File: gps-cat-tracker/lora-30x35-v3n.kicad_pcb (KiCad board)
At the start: 2 copper layers, 31 x 35 mm, 22 parts, among them J1 JST-GH_1.25mm_2P, J2 USB_C_Charge, SW1 MSK12C02, U1 E220-900T22S(JP), U2 ATtiny3226-MFR_VQFN20, U3 MAX-M8Q-00B_LCC18, U4 TP4056

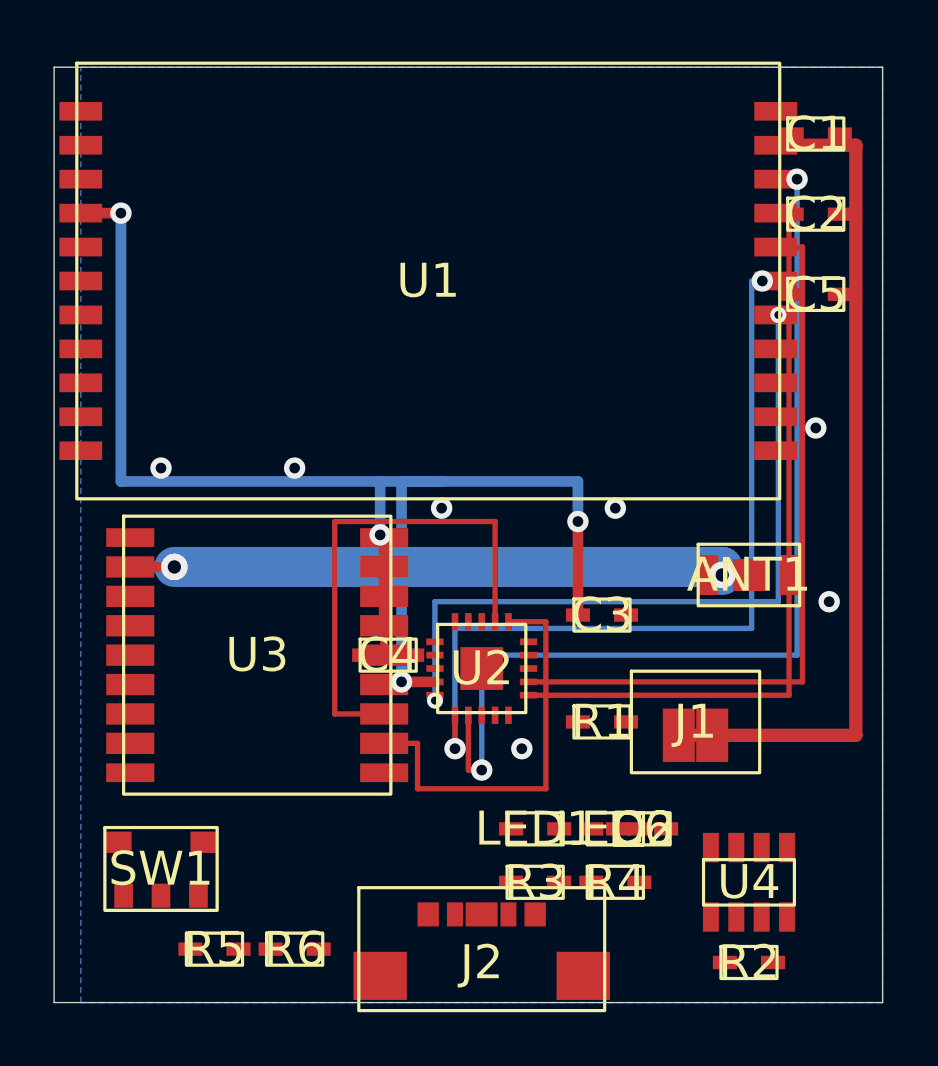
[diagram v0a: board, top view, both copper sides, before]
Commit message: v3n: GNDトレース追加・R1 DNP・B.Cuゾーン塗りつぶし・Gerber更新
- U1.pad11 GND: F.Cu トレース(26.0,1.65)→(27.5,1.65) + ビア追加
- U3 GPS左列 GND: F.Cu トレース(1.85,17.6)→(1.85,26.4) 0.5mm幅追加
- R1(10kΩ) をBOM/CPLから削除（DNP）
- B.Cu GNDゾーン塗りつぶし実行・保存
- Gerber一式再生成（gerber_v3n/）・ZIP更新

Co-Authored-By: Claude Sonnet 4.6 <noreply@anthropic.com>
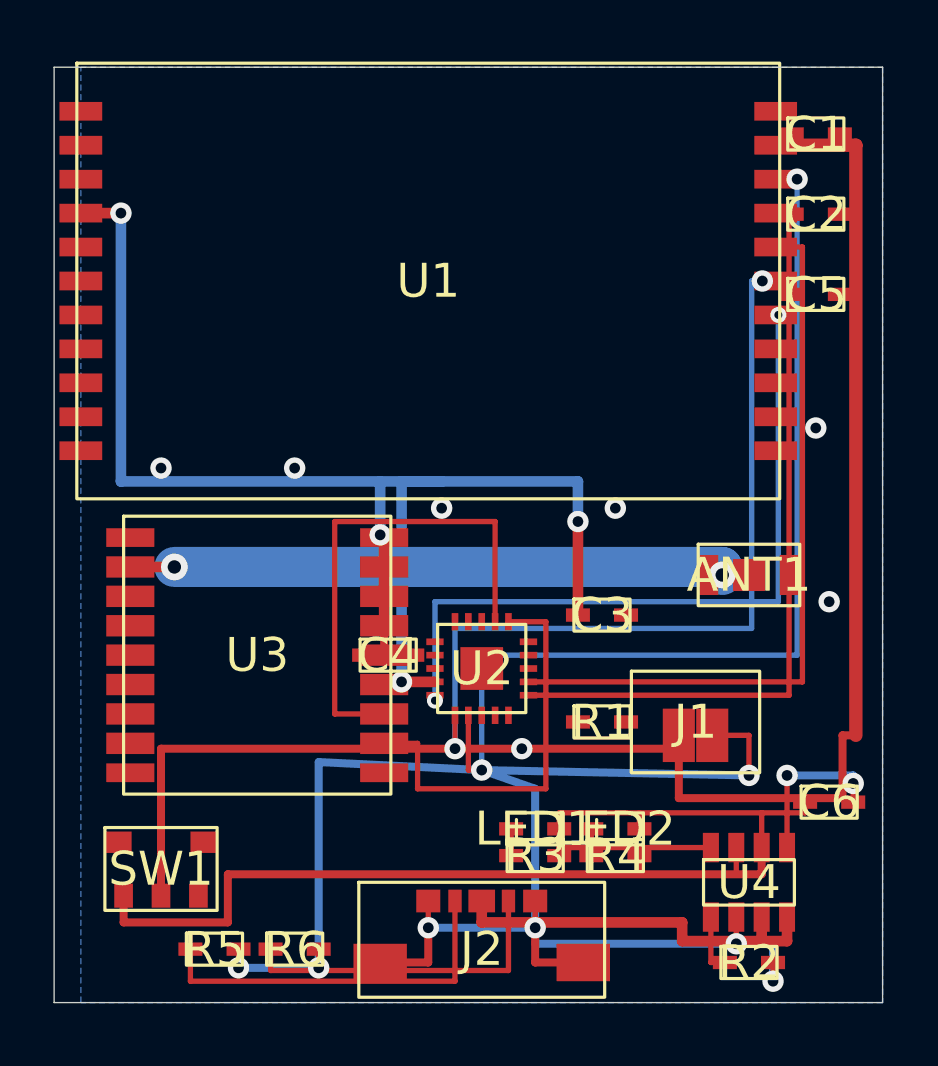
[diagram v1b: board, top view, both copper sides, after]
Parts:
- U3: value MAX-M8Q-00B_LCC18 -> ATGM336H-5N31
- moved C6 7.07 mm to (28.0, 27.5)
- moved R3 1.00 mm to (17.0, 29.5)
- moved R4 1.00 mm to (20.0, 29.5)
- moved J2 0.50 mm to (15.0, 33.0)
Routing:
- net (no net): track 290.1 -> 486.5 mm, vias 19 -> 28
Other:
- board text added: "J2.CC1(A5)→R5(5.1k)→GND / CC2(B5)→R6(5.1k)→GND"
- board text added: "J2.VBUS(AB4)→U4.VCC(3) / J2.GND(A1,B1)→GND"
- board text added: "U4.BAT(6)→SW1.pin1 / SW1.pin2→J1.BATT+→E220.VCC"
- board text added: "U4.CE(4)→VCC / TEMP(5)→GND / C6(100nF)→U4.VCC近傍"
- board text added: "U4.CHRG(8)→R3(330R)→LED1(-) LED1(+)→U4.BAT(VBAT≈3.7V)"
- board text added: "U4.PROG(1)→R2(5k)→GND [1000/5000=200mA]"
- board text added: "U4.STDBY(7)→R4(100R)→LED2(-) LED2(+)→U4.BAT(VBAT≈3.7V) ★R4=100Ω"
- board text removed: "J2.CC1(A5)→R5→GND"
- board text removed: "J2.CC2(B5)→R6→GND"
- board text removed: "J2.GND→GND"
- board text removed: "J2.VBUS→U4.VCC(3)"
- board text removed: "SW1.pin2→J1.BATT+ SW1.pin3=NC"
- board text removed: "U4.BAT(6)→SW1.pin1→J1.BATT+→E220.VCC"
- board text removed: "U4.CE(4)→VCC / TEMP(5)→GND"
- board text removed: "U4.CHRG(8)→R3→LED1(-) / LED1(+)→VCC"
- board text removed: "U4.PROG(1)→R2(5k)→GND [200mA]"
- board text removed: "U4.STDBY(7)→R4→LED2(-) / LED2(+)→VCC"

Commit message: v3n: Bug1/Bug3修正・C2/C4/C5位置修正・DRC 363→349件
- Bug1: via(13.25,23.7) + B.Cu trace(13.25,20→23.7) 削除（ATtiny pad5短絡）
- Bug3: B.Cu (12,15.5)→(12,23) を F.Cu迂回に分割（B.Cu RF/VCC交差解消）
- C4: (11.5,22,0°)→(12.9,17,90°) U3.pad5との0mm接触を解消
- C2: (27.5,5.5,0°)→(28.5,4.5,90°) U1.pad8との0mm接触を解消
- C5: (27.5,8.5,0°)→(28.5,7.5,90°) U1.pad6との0mm接触を解消
- 各バイパスコンデンサにVCC/GNDトレース追加
- 孤立via×6削除・デッドエンドトレース×3削除
- DRC: clearance 10→2件、via_dangling 4→0件

Co-Authored-By: Claude Sonnet 4.6 <noreply@anthropic.com>
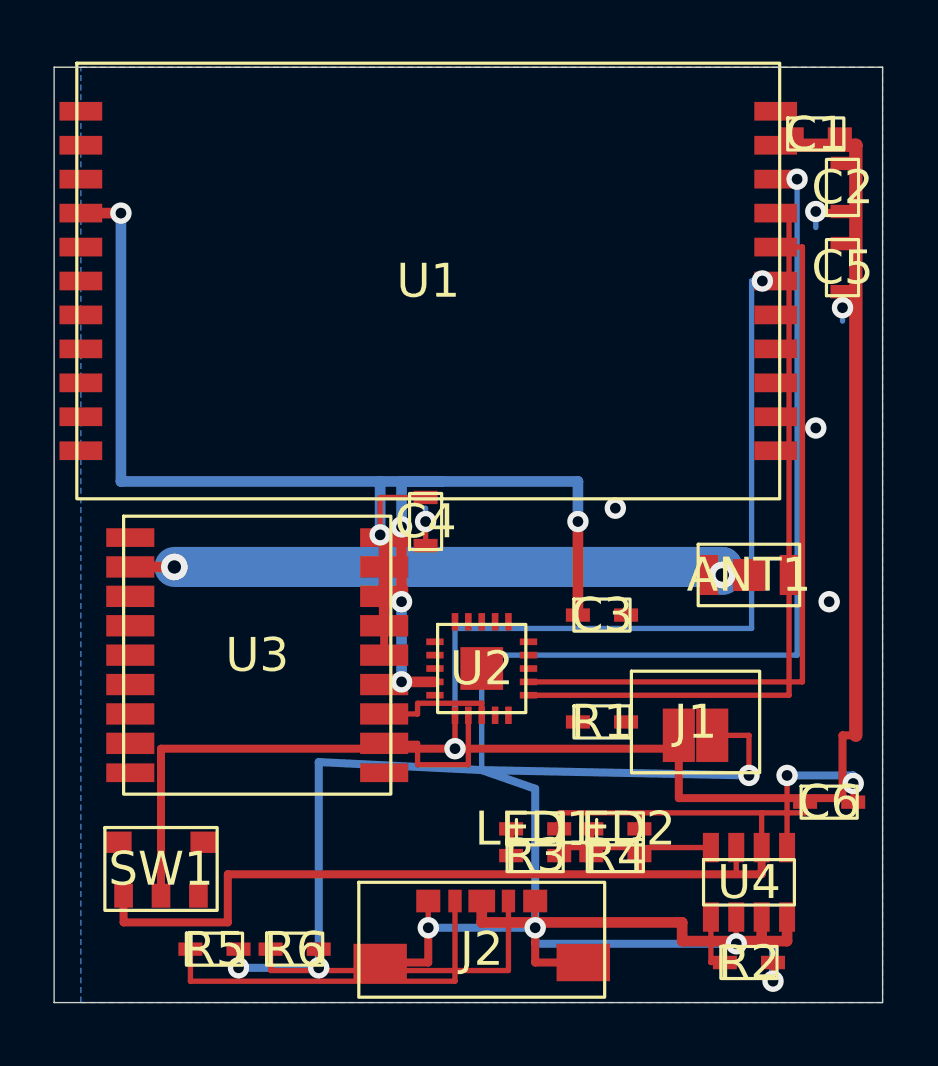
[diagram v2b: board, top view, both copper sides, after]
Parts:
- moved C4 5.19 mm to (12.9, 17.0), turned to 90 degrees
- moved C2 1.41 mm to (28.5, 4.50), turned to 90 degrees
- moved C5 1.41 mm to (28.5, 7.50), turned to 90 degrees
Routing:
- net (no net): track 486.5 -> 440.1 mm, vias 28 -> 26
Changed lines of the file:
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@@
 	(footprint ""
 		(layer "F.Cu")
-		(at 11.5 22)
+		(at 12.9 17 90)
 		(property "Reference" "C4"
 			(at 0 0 0)
@@
 	(footprint ""
 		(layer "F.Cu")
-		(at 27.5 5.5)
+		(at 28.5 4.5 90)
 		(property "Reference" "C2"
 			(at 0 0 0)
@@
 	(footprint ""
 		(layer "F.Cu")
-		(at 27.5 8.5)
+		(at 28.5 7.5 90)
 		(property "Reference" "C5"
 			(at 0 0 0)
@@
 	)
 	(segment
+		(start 15 23.8)
+		(end 15 24.25)
+		(width 0.2)
+		(layer "F.Cu")
+		(net "")
+	)
+	(segment
 		(start 27.1 27.9)
 		(end 27.1 27.5)
@@
 	)
 	(segment
+		(start 12.9 17.9)
+		(end 12.9 17)
+		(width 0.2)
+		(layer "F.Cu")
+		(net "")
+	)
+	(segment
 		(start 23.575 29.2)
 		(end 17.9 29.2)
@@
 	)
 	(segment
-		(start 17.4 27)
-		(end 17.4 20.75)
-		(width 0.2)
-		(layer "F.Cu")
-		(net "")
-	)
-	(segment
 		(start 25.475 29.2)
 		(end 25.475 27.9)
@@
 	)
 	(segment
+		(start 12.6 25.3)
+		(end 12.6 26.1)
+		(width 0.2)
+		(layer "F.Cu")
+		(net "")
+	)
+	(segment
 		(start 15 32)
 		(end 22.5 32)
@@
 	)
 	(segment
+		(start 12.6 23.8)
+		(end 15 23.8)
+		(width 0.2)
+		(layer "F.Cu")
+		(net "")
+	)
+	(segment
 		(start 26.5 23.5)
 		(end 16.75 23.5)
@@
 	)
 	(segment
-		(start 26 9.27)
-		(end 26.1 9.27)
-		(width 0.2)
-		(layer "F.Cu")
-		(net "")
-	)
-	(segment
-		(start 17.4 20.75)
-		(end 16 20.75)
+		(start 12.6 24.2)
+		(end 12.6 23.8)
 		(width 0.2)
 		(layer "F.Cu")
@@
 	)
 	(segment
+		(start 12 17.2)
+		(end 12 20)
+		(width 0.4)
+		(layer "F.Cu")
+		(net "")
+	)
+	(segment
 		(start 15 31.2)
 		(end 15 32)
@@
 	)
 	(segment
+		(start 28.5 6.6)
+		(end 29 6.6)
+		(width 0.2)
+		(layer "F.Cu")
+		(net "")
+	)
+	(segment
 		(start 23.575 31.8)
 		(end 23.575 33.5)
@@
 	)
 	(segment
+		(start 28.5 3.6)
+		(end 29 3.6)
+		(width 0.2)
+		(layer "F.Cu")
+		(net "")
+	)
+	(segment
 		(start 13 32.2)
 		(end 13 33.5)
@@
 	)
 	(segment
+		(start 11.2 16.1)
+		(end 11.2 17.5)
+		(width 0.2)
+		(layer "F.Cu")
+		(net "")
+	)
+	(segment
 		(start 23.625 25)
 		(end 25 25)
@@
 	)
 	(segment
-		(start 11.35 22)
-		(end 10.6 22)
-		(width 0.3)
+		(start 14.5 26.1)
+		(end 14.5 24.25)
+		(width 0.2)
 		(layer "F.Cu")
 		(net "")
@@
 	)
 	(segment
-		(start 11.35 24.2)
-		(end 9.5 24.2)
-		(width 0.2)
-		(layer "F.Cu")
-		(net "")
-	)
-	(segment
 		(start 29 25)
 		(end 29 2.92)
@@
 	)
 	(segment
-		(start 9.5 17)
-		(end 15.5 17)
-		(width 0.2)
-		(layer "F.Cu")
-		(net "")
-	)
-	(segment
-		(start 14.5 26.3)
-		(end 14.5 24.25)
-		(width 0.2)
-		(layer "F.Cu")
-		(net "")
-	)
-	(segment
 		(start 26 4.19)
 		(end 26.8 4.19)
@@
 	)
 	(segment
-		(start 15.5 17)
-		(end 15.5 20.75)
+		(start 4.1 34.2)
+		(end 4.1 33)
 		(width 0.2)
 		(layer "F.Cu")
@@
 	)
 	(segment
-		(start 4.1 34.2)
-		(end 4.1 33)
+		(start 28.5 5.4)
+		(end 27.5 5.4)
 		(width 0.2)
 		(layer "F.Cu")
@@
 	)
 	(segment
-		(start 15 26.3)
-		(end 14.5 26.3)
+		(start 12.6 26.1)
+		(end 14.5 26.1)
 		(width 0.2)
 		(layer "F.Cu")
@@
 	)
 	(segment
-		(start 9.5 24.2)
-		(end 9.5 17)
+		(start 11.35 24.2)
+		(end 12.6 24.2)
 		(width 0.2)
 		(layer "F.Cu")
@@
 	)
 	(segment
-		(start 12.6 25.3)
-		(end 12.6 27)
+		(start 12.9 16.1)
+		(end 11.2 16.1)
 		(width 0.2)
 		(layer "F.Cu")
@@
 	)
 	(segment
+		(start 28.5 8.4)
+		(end 28.5 9)
+		(width 0.2)
+		(layer "F.Cu")
+		(net "")
+	)
+	(segment
 		(start 16 31.2)
 		(end 16 33.8)
@@
 	)
 	(segment
-		(start 12.6 27)
-		(end 17.4 27)
-		(width 0.2)
-		(layer "F.Cu")
-		(net "")
-	)
-	(segment
 		(start 1.6 32)
 		(end 1.6 31)
@@
 	)
 	(via
-		(at 3 15)
+		(at 26.425 26.5)
 		(size 0.8)
 		(drill 0.4)
@@
 	)
 	(via
-		(at 26.425 26.5)
+		(at 25.9 34.2)
 		(size 0.8)
 		(drill 0.4)
@@
 	)
 	(via
-		(at 25.9 34.2)
+		(at 12 20)
 		(size 0.8)
 		(drill 0.4)
@@
 	)
 	(via
-		(at 13.25 23.7)
-		(size 0.6)
-		(drill 0.3)
+		(at 11.2 17.5)
+		(size 0.8)
+		(drill 0.4)
 		(layers "F.Cu" "B.Cu")
 		(net "")
 	)
 	(via
-		(at 11.2 17.5)
+		(at 28.5 9)
 		(size 0.8)
 		(drill 0.4)
@@
 	)
 	(via
-		(at 15 26.3)
+		(at 12.9 17)
 		(size 0.8)
 		(drill 0.4)
@@
 	)
 	(via
-		(at 16.5 25.5)
-		(size 0.8)
-		(drill 0.4)
-		(layers "F.Cu" "B.Cu")
-		(net "")
-	)
-	(via
 		(at 28.9 26.8)
 		(size 0.8)
@@
 	)
 	(via
-		(at 13.5 16.5)
+		(at 12 17.2)
 		(size 0.8)
 		(drill 0.4)
@@
 	)
 	(via
-		(at 26.1 9.27)
-		(size 0.6)
-		(drill 0.3)
-		(layers "F.Cu" "B.Cu")
-		(net "")
-	)
-	(via
 		(at 1.5 5.46)
 		(size 0.8)
@@
 	)
 	(via
-		(at 8 15)
+		(at 27.5 5.4)
 		(size 0.8)
 		(drill 0.4)
@@
 	)
 	(segment
-		(start 26.1 20)
-		(end 13.25 20)
+		(start 26.8 4.19)
+		(end 26.8 22)
 		(width 0.2)
 		(layer "B.Cu")
@@
 	)
 	(segment
-		(start 26.8 4.19)
-		(end 26.8 22)
+		(start 28.5 9)
+		(end 28.5 9.5)
 		(width 0.2)
 		(layer "B.Cu")
@@
 	)
 	(segment
-		(start 26.1 9.27)
-		(end 26.1 20)
+		(start 12.9 17)
+		(end 12.9 16.5)
 		(width 0.2)
 		(layer "B.Cu")
@@
 	)
 	(segment
-		(start 13.25 20)
-		(end 13.25 23.7)
-		(width 0.2)
-		(layer "B.Cu")
-		(net "")
-	)
-	(segment
-		(start 12 15.5)
-		(end 12 23)
-		(width 0.4)
-		(layer "B.Cu")
-		(net "")
-	)
-	(segment
 		(start 13.5 15.5)
 		(end 18.6 15.5)
@@
 	)
 	(segment
+		(start 27.5 5.4)
+		(end 27.5 6)
+		(width 0.2)
+		(layer "B.Cu")
+		(net "")
+	)
+	(segment
 		(start 11.2 15.5)
 		(end 11.2 17.5)
@@
 	)
 	(segment
+		(start 12 20)
+		(end 12 23)
+		(width 0.4)
+		(layer "B.Cu")
+		(net "")
+	)
+	(segment
 		(start 5.9 33.7)
 		(end 8.9 33.7)
@@
 		(layer "B.Cu")
 		(net "")
+	)
+	(segment
+		(start 12 15.5)
+		(end 12 17.2)
+		(width 0.4)
+		(layer "B.Cu")
+		(net "")

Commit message: v3n: Bug5修正・C1/J1/TP1-3・R1DNP適用・DRC clearance0・Gerber更新
- Bug5 (ATtiny VDD未接続): F.Cu(12,23)→(13.25,23)削除・via(12,23)削除
  B.Cu(12,20)→(12,23)削除・B.Cu VCC(13.5,15.5→13.5,21.1)+via(13.5,21.1)追加
- C1移動: (27.5,2.5)→(27.5,0.8) + VCCトレース + GND via
- J1パッド幅: 1.2→1.0mm (clearance確保)
- TP1(UPDI)/TP2(VCC)/TP3(GND) テストパッド追加
- R1 DNP設定
- DRC: clearance 0件・未配線 0件・358件
- Gerber: gerber_jlcpcb_final.zip (JLCPCB標準拡張子・18KB)

Co-Authored-By: Claude Sonnet 4.6 <noreply@anthropic.com>
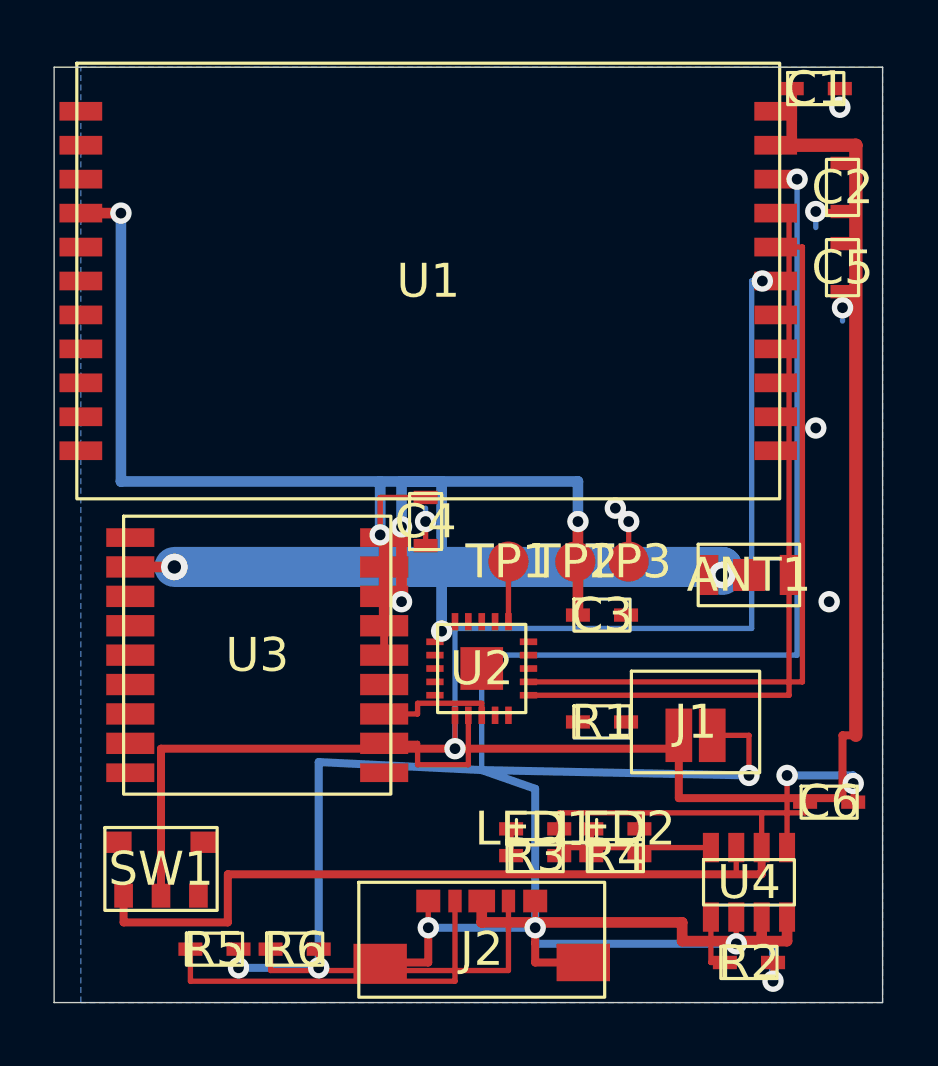
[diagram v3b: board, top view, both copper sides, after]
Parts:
- added TP1: , , F.Cu at (16.0, 18.5)
- added TP2: , , F.Cu at (18.5, 18.5)
- added TP3: , , F.Cu at (20.5, 18.5)
- moved C1 1.70 mm to (27.5, 0.80)
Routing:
- net (no net): track 440.1 -> 448.9 mm, vias 26 -> 28
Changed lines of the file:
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@@
 	(footprint ""
 		(layer "F.Cu")
+		(at 18.5 18.5)
+		(property "Reference" "TP2"
+			(at 0 0 0)
+			(layer "F.SilkS")
+			(effects
+				(font
+					(size 1.27 1.27)
+				)
+			)
+		)
+		(property "Value" ""
+			(at 0 0 0)
+			(layer "F.Fab")
+			(effects
+				(font
+					(size 1.27 1.27)
+				)
+			)
+		)
+		(property "Datasheet" ""
+			(at 0 0 0)
+			(layer "F.Fab")
+			(hide yes)
+			(effects
+				(font
+					(size 1.27 1.27)
+				)
+			)
+		)
+		(property "Description" ""
+			(at 0 0 0)
+			(layer "F.Fab")
+			(hide yes)
+			(effects
+				(font
+					(size 1.27 1.27)
+				)
+			)
+		)
+		(duplicate_pad_numbers_are_jumpers no)
+		(pad "1" smd circle
+			(at 0 0)
+			(size 1.5 1.5)
+			(layers "F.Cu" "F.Mask" "F.Paste")
+		)
+		(embedded_fonts no)
+	)
+	(footprint ""
+		(layer "F.Cu")
 		(at 25 33.5)
 		(property "Reference" "R2"
@@
 	(footprint ""
 		(layer "F.Cu")
-		(at 27.5 2.5)
+		(at 16 18.5)
+		(property "Reference" "TP1"
+			(at 0 0 0)
+			(layer "F.SilkS")
+			(effects
+				(font
+					(size 1.27 1.27)
+				)
+			)
+		)
+		(property "Value" ""
+			(at 0 0 0)
+			(layer "F.Fab")
+			(effects
+				(font
+					(size 1.27 1.27)
+				)
+			)
+		)
+		(property "Datasheet" ""
+			(at 0 0 0)
+			(layer "F.Fab")
+			(hide yes)
+			(effects
+				(font
+					(size 1.27 1.27)
+				)
+			)
+		)
+		(property "Description" ""
+			(at 0 0 0)
+			(layer "F.Fab")
+			(hide yes)
+			(effects
+				(font
+					(size 1.27 1.27)
+				)
+			)
+		)
+		(duplicate_pad_numbers_are_jumpers no)
+		(pad "1" smd circle
+			(at 0 0)
+			(size 1.5 1.5)
+			(layers "F.Cu" "F.Mask" "F.Paste")
+		)
+		(embedded_fonts no)
+	)
+	(footprint ""
+		(layer "F.Cu")
+		(at 27.5 0.8)
 		(property "Reference" "C1"
 			(at 0 0 0)
@@
 			)
 		)
+		(attr dnp)
 		(duplicate_pad_numbers_are_jumpers no)
 		(fp_rect
@@
 		(pad "1" smd rect
 			(at -0.625 0.5)
-			(size 1.2 2)
+			(size 1 2)
 			(layers "F.Cu" "F.Mask" "F.Paste")
 			(thermal_bridge_angle 45)
@@
 		(pad "2" smd rect
 			(at 0.625 0.5)
-			(size 1.2 2)
+			(size 1 2)
 			(layers "F.Cu" "F.Mask" "F.Paste")
 			(thermal_bridge_angle 45)
@@
 		(embedded_fonts no)
 	)
+	(footprint ""
+		(layer "F.Cu")
+		(at 20.5 18.5)
+		(property "Reference" "TP3"
+			(at 0 0 0)
+			(layer "F.SilkS")
+			(effects
+				(font
+					(size 1.27 1.27)
+				)
+			)
+		)
+		(property "Value" ""
+			(at 0 0 0)
+			(layer "F.Fab")
+			(effects
+				(font
+					(size 1.27 1.27)
+				)
+			)
+		)
+		(property "Datasheet" ""
+			(at 0 0 0)
+			(layer "F.Fab")
+			(hide yes)
+			(effects
+				(font
+					(size 1.27 1.27)
+				)
+			)
+		)
+		(property "Description" ""
+			(at 0 0 0)
+			(layer "F.Fab")
+			(hide yes)
+			(effects
+				(font
+					(size 1.27 1.27)
+				)
+			)
+		)
+		(duplicate_pad_numbers_are_jumpers no)
+		(pad "1" smd circle
+			(at 0 0)
+			(size 1.5 1.5)
+			(layers "F.Cu" "F.Mask" "F.Paste")
+		)
+		(embedded_fonts no)
+	)
 	(gr_rect
 		(start -1 0)
@@
 	)
 	(segment
+		(start 16 20.75)
+		(end 16 18.5)
+		(width 0.2)
+		(layer "F.Cu")
+		(net "")
+	)
+	(segment
 		(start 23.575 31.8)
 		(end 23.575 33.5)
@@
 	)
 	(segment
+		(start 20.5 18.5)
+		(end 20.5 17)
+		(width 0.2)
+		(layer "F.Cu")
+		(net "")
+	)
+	(segment
 		(start 11.35 25.3)
 		(end 12.6 25.3)
@@
 	)
 	(segment
+		(start 18.5 18.5)
+		(end 18.6 17)
+		(width 0.2)
+		(layer "F.Cu")
+		(net "")
+	)
+	(segment
 		(start 19.1 29.5)
 		(end 19.1 28.5)
@@
 	)
 	(segment
-		(start 12 23)
-		(end 13.25 23)
-		(width 0.4)
-		(layer "F.Cu")
-		(net "")
-	)
-	(segment
 		(start 11.2 16.1)
 		(end 11.2 17.5)
@@
 	)
 	(segment
+		(start 26.6 0.8)
+		(end 26.6 2.92)
+		(width 0.4)
+		(layer "F.Cu")
+		(net "")
+	)
+	(segment
 		(start 26 4.19)
 		(end 26.8 4.19)
@@
 	)
 	(via
-		(at 12 23)
-		(size 0.8)
-		(drill 0.4)
-		(layers "F.Cu" "B.Cu")
-		(net "")
-	)
-	(via
 		(at 17 32.2)
 		(size 0.8)
@@
 	)
 	(via
+		(at 13.5 21.1)
+		(size 0.8)
+		(drill 0.4)
+		(layers "F.Cu" "B.Cu")
+		(net "")
+	)
+	(via
 		(at 12 20)
 		(size 0.8)
@@
 	)
 	(via
+		(at 18.6 17)
+		(size 0.8)
+		(drill 0.4)
+		(layers "F.Cu" "B.Cu")
+		(net "")
+	)
+	(via
 		(at 28 20)
 		(size 0.8)
@@
 	)
 	(via
+		(at 28.4 1.5)
+		(size 0.8)
+		(drill 0.4)
+		(layers "F.Cu" "B.Cu")
+		(net "")
+	)
+	(via
 		(at 1.5 5.46)
 		(size 0.8)
@@
 	)
 	(via
-		(at 18.6 17)
+		(at 24.525 32.8)
 		(size 0.8)
 		(drill 0.4)
@@
 	)
 	(via
-		(at 24.525 32.8)
+		(at 20.5 17)
 		(size 0.8)
 		(drill 0.4)
@@
 	)
 	(segment
+		(start 13.5 15.5)
+		(end 13.5 21.1)
+		(width 0.4)
+		(layer "B.Cu")
+		(net "")
+	)
+	(segment
 		(start 25.9 32.8)
 		(end 25.9 34.2)
@@
 		(layer "B.Cu")
 		(net "")
-	)
-	(segment
-		(start 12 20)
-		(end 12 23)
-		(width 0.4)
-		(layer "B.Cu")
-		(net "")
